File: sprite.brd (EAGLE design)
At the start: 35 x 35 mm, 40 parts

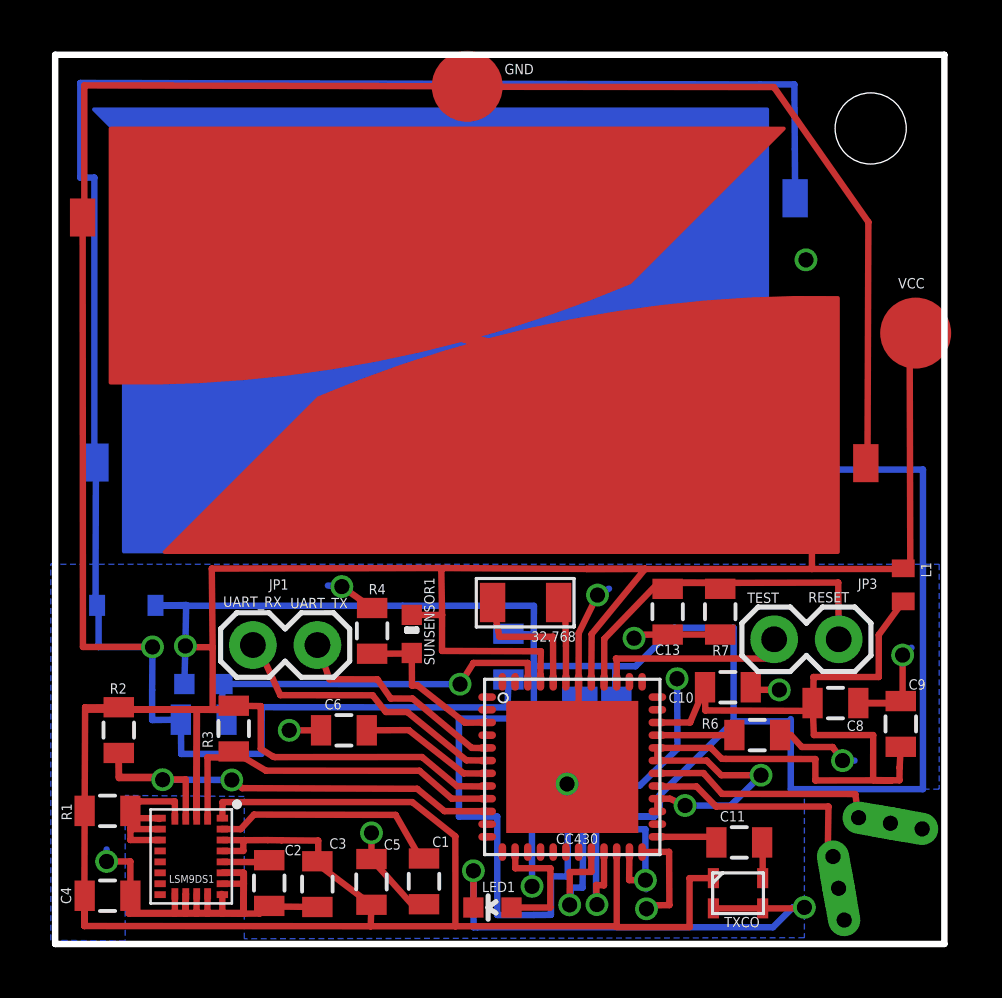
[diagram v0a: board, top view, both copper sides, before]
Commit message: added Gerbers, fixed DRC errors
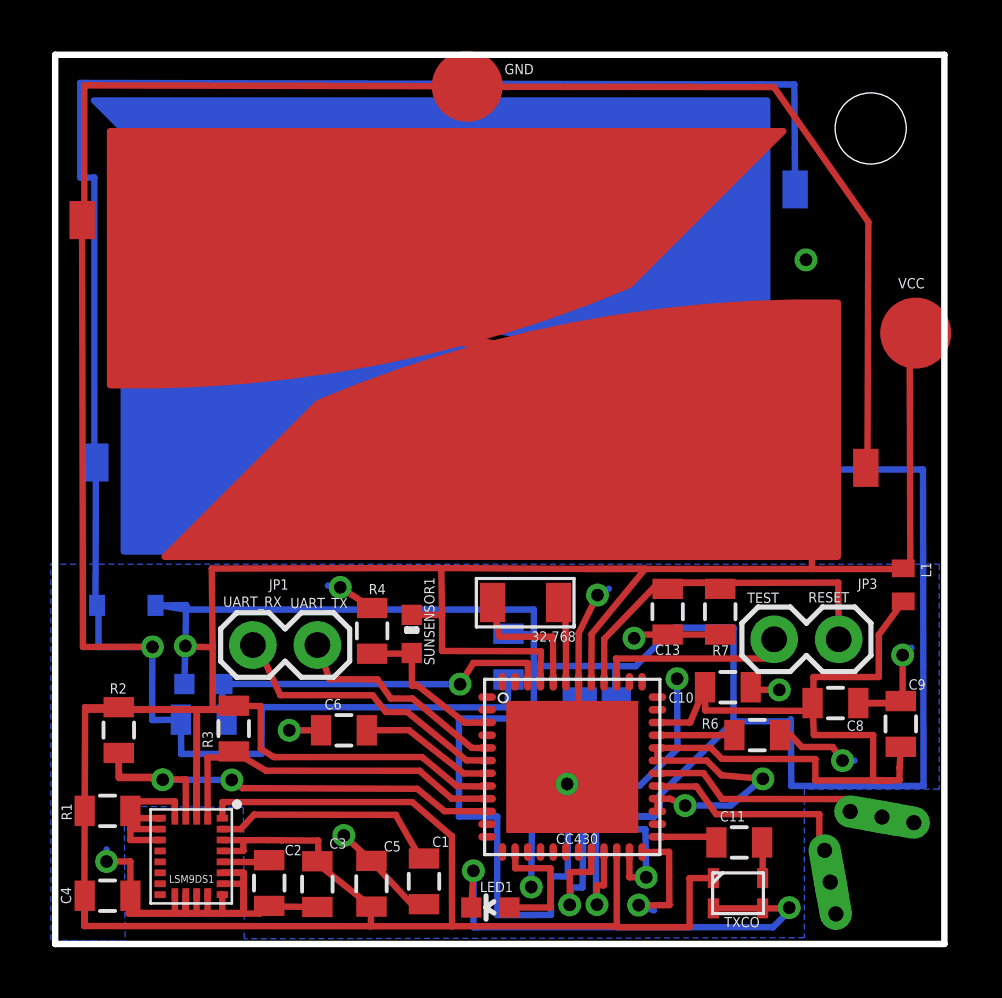
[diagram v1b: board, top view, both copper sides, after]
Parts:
- moved U$2 0.41 mm to (32.5, 5.00)
- moved ANT_1 0.41 mm to (30.5, 2.44)
- moved U$10 0.35 mm to (28.0, 33.2)
- moved U$11 0.19 mm to (30.8, 15.2)
- moved U$9 0.10 mm to (2.16, 32.0)
- moved LED1 0.08 mm to (17.1, 1.44)
- moved C5 0.07 mm to (12.5, 2.37)
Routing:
- net ANT1: track 11.8 -> 11.2 mm
- net P2.6: track 4.47 -> 5.01 mm
